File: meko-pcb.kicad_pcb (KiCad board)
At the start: 2 copper layers, 258.5 x 149 mm, 60 parts, among them IC1 ES9218PQ, IC2 AS5600-ASOM, IC3 LP5912-3.3DRVR, J1 GDEY0154D67, J2 MEM2090-00-145-00-A, J3 USB_C_Receptacle_USB2.0_16P, J4 Conn_ARM_SWD_TagConnect_TC2030, J5 SJ2-35954B-SMT-TR, Q1 SS8050, Q2 SS8050, Q3 Si1308EDL, U1 ESP32-PICO-MINI-02, U12 BQ24075RGT, U2 LP5907SNX-1.8/NOPB, U3 LP5907SNX-3.3/NOPB, U5 USBLC6-2SC6, U6 LP5907SNX-3.3/NOPB, U7 LP5907SNX-3.3/NOPB, U8 CP2102N-Axx-xQFN24, Y2 ECS-2520SMV-500-GP-TR

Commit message: esd, jack, io expander, led, power swquence
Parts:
- removed J4: Conn_ARM_SWD_TagConnect_TC2030, Connector:Tag-Connect_TC2030-IDC-FP_2x03_P1.27mm_Vertical
- removed JP9: SolderJumper_2_Bridged, Jumper:SolderJumper-2_P1.3mm_Bridged_RoundedPad1.0x1.5mm
- removed TP12, TP13, TP14: TestPoint, TestPoint:TestPoint_Pad_D1.5mm
- added D10: D_TVS, Diode_SMD:D_0201_0603Metric, F.Cu at (228.7, 158.2)
- added D11: D_TVS, Diode_SMD:D_0201_0603Metric, F.Cu at (228.7, 160.0)
- added D5: D3V3X8U9LP3810, Package_DFN_QFN:Diodes_UDFN3810-9_TYPE_B, F.Cu at (174.0, 52.0)
- added D6: D3V3X8U9LP3810, Package_DFN_QFN:Diodes_UDFN3810-9_TYPE_B, F.Cu at (177.1, 52.0)
- added D7: SK6805, LED_SMD:LED_SK6805_PLCC4_2.4x2.7mm_P1.3mm, F.Cu at (148.5, 151.3)
- added D8: D_TVS, Diode_SMD:D_0201_0603Metric, F.Cu at (203.2, 135.0)
- added D9: D_TVS, Diode_SMD:D_0201_0603Metric, F.Cu at (228.7, 156.5)
- added IC4: TCAL9538RSVR, TCAL9538RSVR:QFN40P180X260X55-16N, F.Cu at (180.5, 51.6)
- added JP10: SolderJumper_2_Open, Jumper:SolderJumper-2_P1.3mm_Open_RoundedPad1.0x1.5mm, F.Cu at (174.5, 69.5)
- added U4: LP5907SNX-1.8/NOPB, Package_SON:Texas_X2SON-4_1x1mm_P0.65mm, F.Cu at (178.3, 61.9)
- JP2, JP3, JP4: value SolderJumper_2_Bridged -> SolderJumper_2_Open; footprint Jumper:SolderJumper-2_P1.3mm_Bridged_RoundedPad1.0x1.5mm -> Jumper:SolderJumper-2_P1.3mm_Open_RoundedPad1.0x1.5mm
- moved TP11 110.5 mm to (180.3, 55.8)
- moved JP4 97.9 mm to (183.9, 62.4)
- moved JP2 87.4 mm to (174.5, 62.4)
- moved JP3 87.4 mm to (174.5, 65.9)
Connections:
- net /HAL_SCL renamed /I2C_1_SCL
- net /HAL_SDA renamed /I2C_1_SDA
- net /USB/SUSP renamed /PWR_EN_USB
- IC1 pad 22: Net-(IC1-OUT_L) -> /audio/OUT_L
- IC1 pad 9: Net-(IC1-OUT_R) -> /audio/OUT_R
- J1 pad 18: Net-(J1-VDD) -> /DISPL_VDD
- J1 pad 19: unconnected-(J1-VPP-Pad19) -> /DISPL_VPP
- J1 pad 6: unconnected-(J1-TSCL-Pad6) -> /DISPL_TSCL
- J1 pad 7: unconnected-(J1-TSDA-Pad7) -> /DISPL_TSDA
- J3 pad S1: GND -> unconnected-(J3-SHIELD-PadS1)_3
- J5 pad R1: Net-(J5-PadR1) -> /audio/OUT_R
- J5 pad R2: Net-(J5-PadR1) -> GND
- J5 pad S: Net-(J5-PadR1) -> /AUDIO_MIC
- J5 pad T: Net-(J5-PadR1) -> /audio/OUT_L
- J5 pad TN: Net-(J5-PadR1) -> /AUDIO_TN
- JP1 pad 1: /power/EN3V3VCAA -> /power/EN3V3MCLK
- JP2 pad 1: /power/EN3V3MCLK -> /power/REG-OUT
- JP2 pad 2: /power/REG-OUT -> /PWR_EN3V3AVCC
- JP3 pad 1: /power/EN3V3AVCC -> +3V3AVCC
- JP3 pad 2: /power/REG-OUT -> /PWR_EN1V8AVCC
- JP4 pad 1: /power/EN1V8AVCC -> +3V3MCLK
- JP4 pad 2: +3V3AVCC -> /AUDIO_MLCK_EN
- L1 pad 1: +3V3AVCC -> +3V3
- TP11 pad 1: /power/EN1V8AVCC -> /power/EN3V3MCLK
- U1 pad 12: unconnected-(U1-32K_XP/GPIO32/ADC1_CH4-Pad12) -> /EXP_~{INT}
- U1 pad 13: /AUDIO_MLCK_EN -> /HAPTIC_MOTOR
- U1 pad 29: /BTN_SIDE_R -> /EXP_~{RES}
- U1 pad 6: /BTN_SIDE_L -> /AUDIO_MIC
- U1 pad 7: /AUDIO_RESETB -> /LED
- U2 pad 3: /power/EN1V8AVCC -> /PWR_EN1V8AVCC
- U3 pad 3: /power/EN3V3VCAA -> /PWR_EN3V3VCCA
- U7 pad 3: /power/EN3V3AVCC -> /PWR_EN3V3AVCC

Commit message: small fixes
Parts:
- added D1: US1B, Diode_SMD:D_SMA, F.Cu at (204.0, 138.5)
- added Q3: SS8050, Package_TO_SOT_SMD:SOT-23, F.Cu at (114.6, 86.0)
- renumbered C94 to C23, C93 to C24, C92 to C25, C1 to C26, D9 to D11, D8 to D12, D7 to D2, D4 to D3, D3 to D4, D2 to D5, D5 to D6, D6 to D7, D1 to D8, D11 to D9, F2 to F1, IC2 to IC1, IC4 to IC2, IC1 to IC4, J5 to J4, JP7 to JP1, JP8 to JP2, JP6 to JP3, JP5 to JP4, JP1 to JP5, JP10 to JP6, JP2 to JP7, JP3 to JP8, JP4 to JP9, L2 to L1, L1 to L2, Q3 to Q4, R34 to R16, R32 to R17, R30 to R19, R28 to R20, R11 to R25, R12 to R26, TP3 to TP1, TP1 to TP10, TP2 to TP11, TP7 to TP2, TP4 to TP3, TP5 to TP4, TP8 to TP5, TP11 to TP7, TP9 to TP8, TP10 to TP9, U12 to U2, U6 to U3, U3 to U4, U4 to U5, U7 to U6, U2 to U7, U5 to U8, U8 to U9, Y2 to Y1

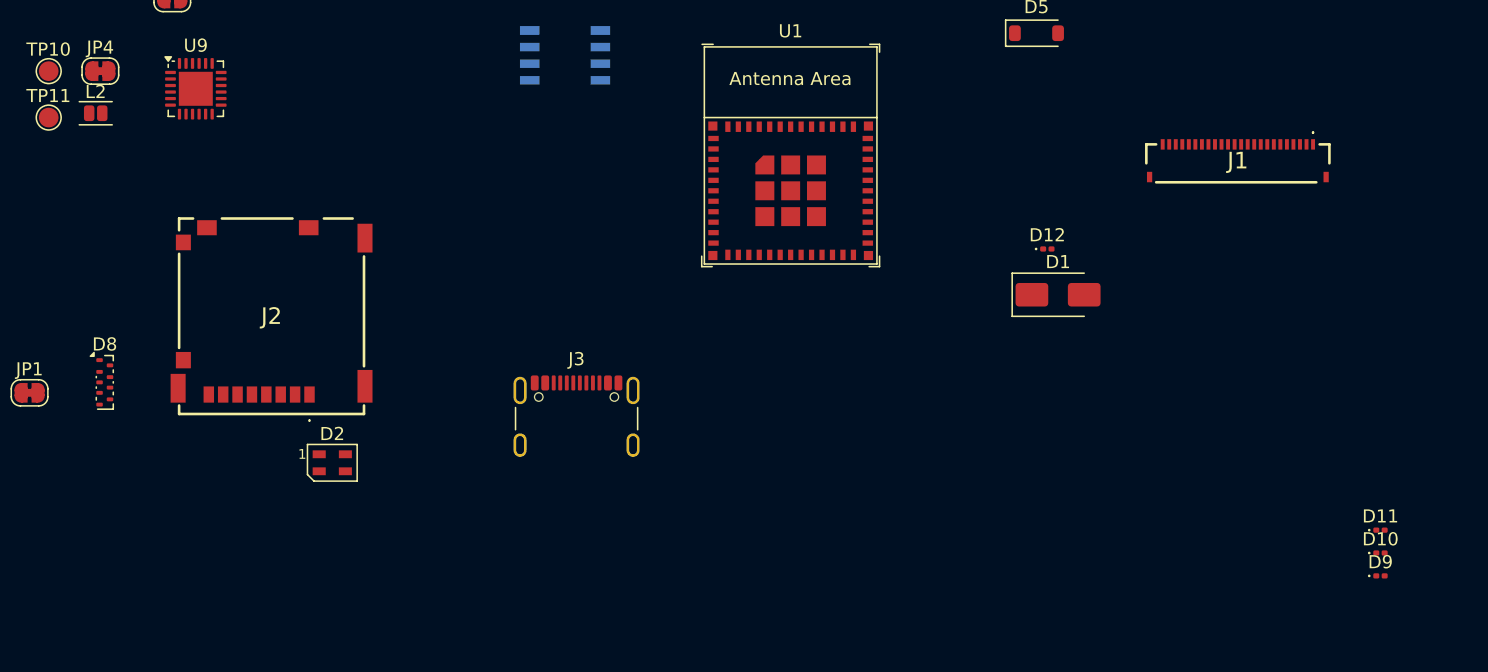
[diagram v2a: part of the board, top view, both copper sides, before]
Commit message: added 3d models
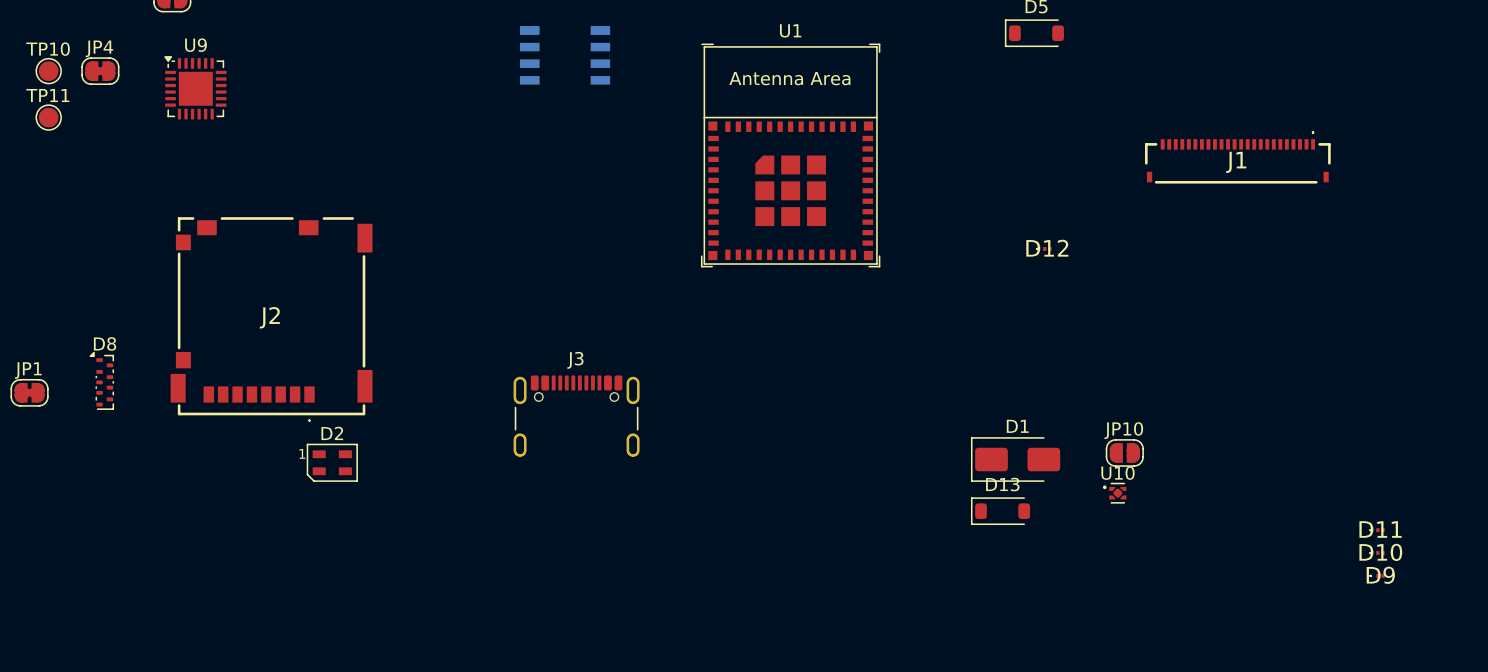
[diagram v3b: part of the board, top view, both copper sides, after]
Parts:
- removed L2: 100uH, Inductor_SMD:L_TDK_MLZ2012_h1.25mm
- added D13: MBR0530, Diode_SMD:D_SOD-123, F.Cu at (199.8, 155.1)
- added JP10: SolderJumper_2_Open, Jumper:SolderJumper-2_P1.3mm_Open_RoundedPad1.0x1.5mm, F.Cu at (209.1, 150.6)
- added U10: LP5907SNX-1.8/NOPB, Package_SON:Texas_X2SON-4_1x1mm_P0.65mm, F.Cu at (208.6, 153.7)
- D10, D11, D12, D9: footprint Diode_SMD:D_0201_0603Metric -> CD0201-T2.0LC:CD0201T20LC
- moved D1 13.0 mm to (200.9, 151.1)
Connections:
- IC1 pad 6: /I2C_1_SDA -> /I2C_SDA
- IC1 pad 7: /I2C_1_SCL -> /I2C_SCL
- IC2 pad 10: /BTN_SIDE_R -> /PWR_EN3V3AVDD
- IC2 pad 12: /I2C_1_SCL -> /I2C_SCL
- IC2 pad 13: /I2C_1_SDA -> /I2C_SDA
- IC2 pad 5: /BTN_SIDE_L -> unconnected-(IC2-P3-Pad5)
- IC4 pad 38: /AUDIO_SCL -> /I2C_SCL
- IC4 pad 39: /AUDIO_SDA -> /I2C_SDA
- Q2 pad 3: /AUDIO_DATA_CLK -> Net-(D13-A)
- U1 pad 26: /I2C_1_SDA -> /I2C_SDA
- U1 pad 33: /I2C_1_SCL -> /I2C_SCL
- U1 pad 34: /AUDIO_DATA_2 -> /BTN_SIDE_L
- U1 pad 35: /AUDIO_DATA1 -> /BTN_SIDE_R

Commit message: fuel gauge ic
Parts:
- added IC5: BQ27427YZFR, BQ27427YZFR:BGA9C50P3X3_158X162X62, F.Cu at (145.5, 67.0)
- added R31: 10k, Resistor_SMD:R_0402_1005Metric, F.Cu at (144.6, 70.3)
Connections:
- net /power/VBAT renamed +BATT
- D13 pad 1: /AUDIO_DATA_CLK -> /AUDIO_DATA_CLK/BOOT
- IC2 pad 5: unconnected-(IC2-P3-Pad5) -> /PWR_FUEL_GPOUT
- U1 pad 15: /AUDIO_SCL -> /AUDIO_DATA1
- U1 pad 16: /AUDIO_SDA -> /AUDIO_DATA1
- U1 pad 23: /AUDIO_DATA_CLK -> /AUDIO_DATA_CLK/BOOT
- U1 pad 27: /MEM_COM -> /LED
- U1 pad 7: /LED -> /MEM_COM

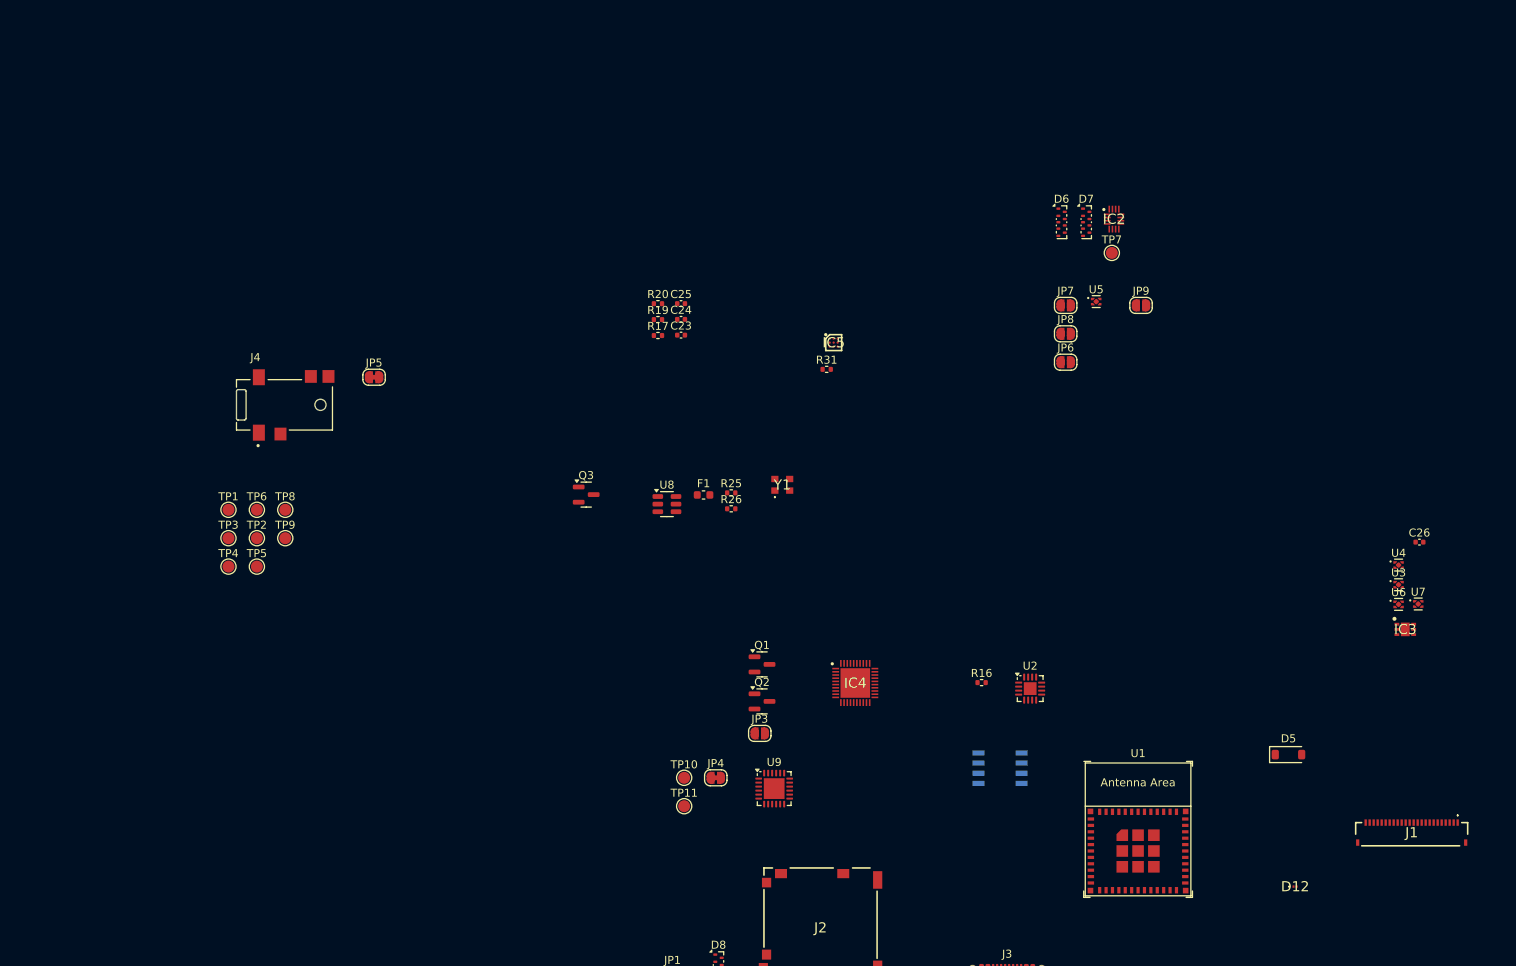
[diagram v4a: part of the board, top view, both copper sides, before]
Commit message: added missing 3d models
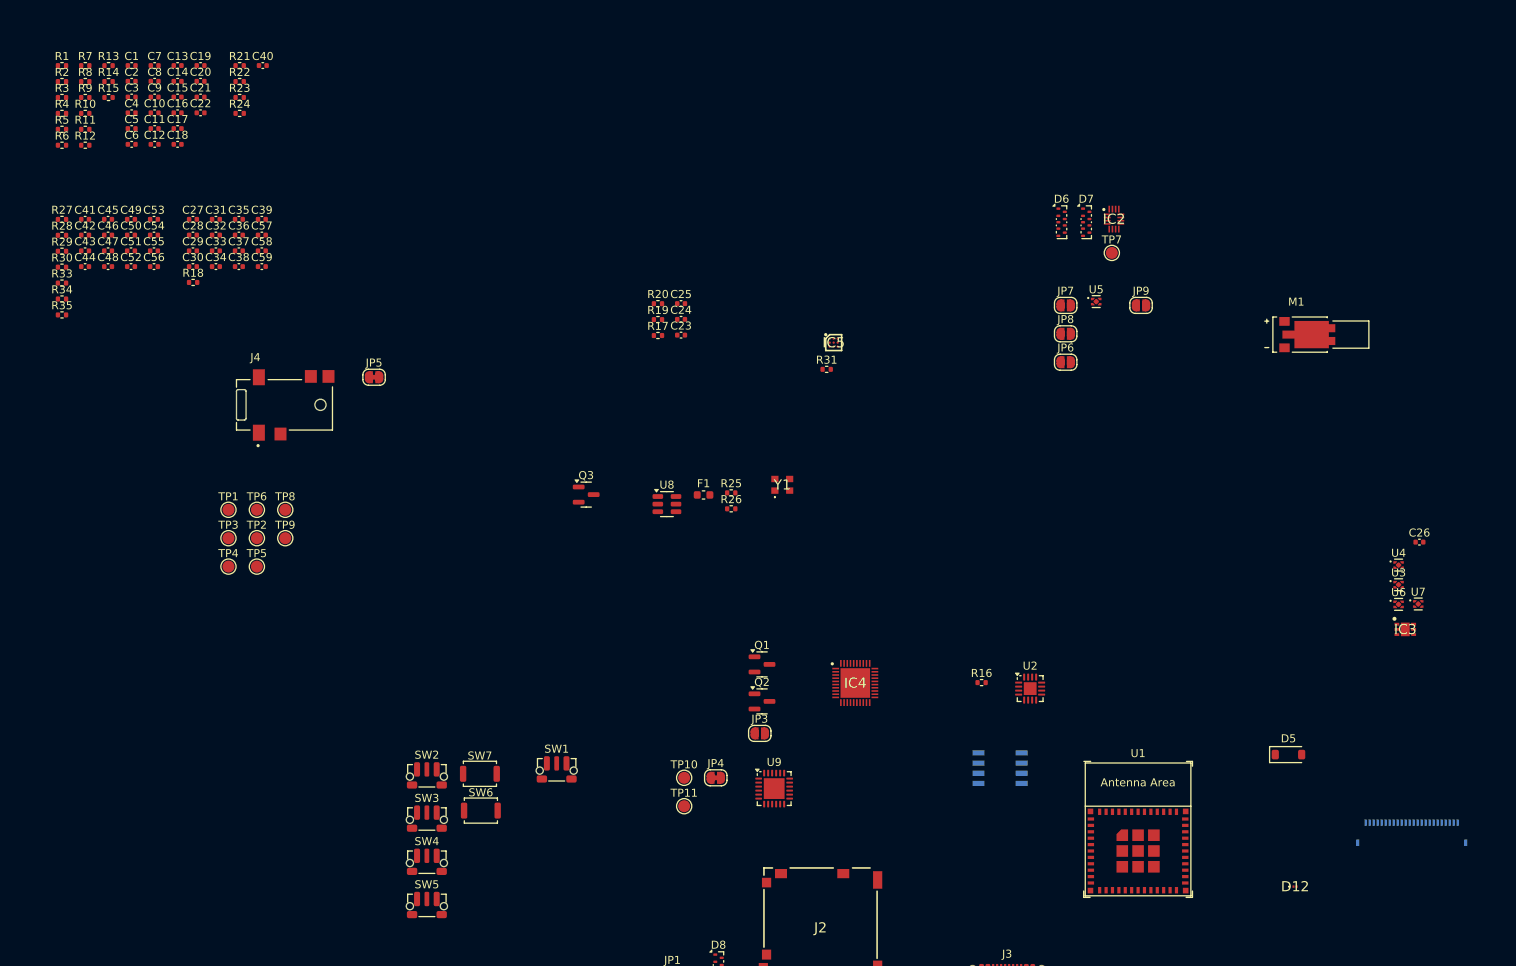
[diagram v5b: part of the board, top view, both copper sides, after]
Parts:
- added C1: 100nF, Capacitor_SMD:C_0402_1005Metric, F.Cu at (57.8, 32.4)
- added C10: 1uF, Capacitor_SMD:C_0402_1005Metric, F.Cu at (60.6, 38.3)
- added C11: 1uF, Capacitor_SMD:C_0402_1005Metric, F.Cu at (60.6, 40.2)
- added C12: 1uF, Capacitor_SMD:C_0402_1005Metric, F.Cu at (60.6, 42.2)
- added C13: 1uF, Capacitor_SMD:C_0402_1005Metric, F.Cu at (63.5, 32.4)
- added C14: 1uF, Capacitor_SMD:C_0402_1005Metric, F.Cu at (63.5, 34.3)
- added C15: 1uF, Capacitor_SMD:C_0402_1005Metric, F.Cu at (63.5, 36.3)
- added C16: 1uF, Capacitor_SMD:C_0402_1005Metric, F.Cu at (63.5, 38.3)
- added C17: 1uF, Capacitor_SMD:C_0402_1005Metric, F.Cu at (63.5, 40.2)
- added C18: 1uF, Capacitor_SMD:C_0402_1005Metric, F.Cu at (63.5, 42.2)
- added C19: 1uF, Capacitor_SMD:C_0402_1005Metric, F.Cu at (66.4, 32.4)
- added C2: 100nF, Capacitor_SMD:C_0402_1005Metric, F.Cu at (57.8, 34.3)
- added C20: 1uF, Capacitor_SMD:C_0402_1005Metric, F.Cu at (66.4, 34.3)
- added C21: 1uF, Capacitor_SMD:C_0402_1005Metric, F.Cu at (66.4, 36.3)
- added C22: 1uF, Capacitor_SMD:C_0402_1005Metric, F.Cu at (66.4, 38.3)
- added C27: 1uF, Capacitor_SMD:C_0402_1005Metric, F.Cu at (65.4, 51.6)
- added C28: 1uF, Capacitor_SMD:C_0402_1005Metric, F.Cu at (65.4, 53.6)
- added C29: 1uF, Capacitor_SMD:C_0402_1005Metric, F.Cu at (65.4, 55.5)
- added C3: 100nF, Capacitor_SMD:C_0402_1005Metric, F.Cu at (57.8, 36.3)
- added C30: 1uF, Capacitor_SMD:C_0402_1005Metric, F.Cu at (65.4, 57.5)
- added C31: 1uF, Capacitor_SMD:C_0402_1005Metric, F.Cu at (68.3, 51.6)
- added C32: 1uF, Capacitor_SMD:C_0402_1005Metric, F.Cu at (68.3, 53.6)
- added C33: 1uF, Capacitor_SMD:C_0402_1005Metric, F.Cu at (68.3, 55.5)
- added C34: 1uF, Capacitor_SMD:C_0402_1005Metric, F.Cu at (68.3, 57.5)
- added C35: 1uF, Capacitor_SMD:C_0402_1005Metric, F.Cu at (71.2, 51.6)
- added C36: 1uF, Capacitor_SMD:C_0402_1005Metric, F.Cu at (71.2, 53.6)
- added C37: 1uF, Capacitor_SMD:C_0402_1005Metric, F.Cu at (71.2, 55.5)
- added C38: 1uF, Capacitor_SMD:C_0402_1005Metric, F.Cu at (71.2, 57.5)
- added C39: 1uF, Capacitor_SMD:C_0402_1005Metric, F.Cu at (74.0, 51.6)
- added C4: 100nF, Capacitor_SMD:C_0402_1005Metric, F.Cu at (57.8, 38.3)
- added C40: 10uF, Capacitor_SMD:C_0402_1005Metric, F.Cu at (74.1, 32.4)
- added C41: 1uF, Capacitor_SMD:C_0402_1005Metric, F.Cu at (51.9, 51.6)
- added C42: 22uF, Capacitor_SMD:C_0402_1005Metric, F.Cu at (51.9, 53.6)
- added C43: 1uF, Capacitor_SMD:C_0402_1005Metric, F.Cu at (51.9, 55.5)
- added C44: 1uF, Capacitor_SMD:C_0402_1005Metric, F.Cu at (51.9, 57.5)
- added C45: 1uF, Capacitor_SMD:C_0402_1005Metric, F.Cu at (54.8, 51.6)
- added C46: 4.7uF, Capacitor_SMD:C_0402_1005Metric, F.Cu at (54.8, 53.6)
- added C47: 4.7uF, Capacitor_SMD:C_0402_1005Metric, F.Cu at (54.8, 55.5)
- added C48: 4.7uF, Capacitor_SMD:C_0402_1005Metric, F.Cu at (54.8, 57.5)
- added C49: 4.7uF, Capacitor_SMD:C_0402_1005Metric, F.Cu at (57.7, 51.6)
- added C5: 100nF, Capacitor_SMD:C_0402_1005Metric, F.Cu at (57.8, 40.2)
- added C50: 4.7uF, Capacitor_SMD:C_0402_1005Metric, F.Cu at (57.7, 53.6)
- added C51: 2.2uF, Capacitor_SMD:C_0402_1005Metric, F.Cu at (57.7, 55.5)
- added C52: 1uF, Capacitor_SMD:C_0402_1005Metric, F.Cu at (57.7, 57.5)
- added C53: 2.2nF, Capacitor_SMD:C_0402_1005Metric, F.Cu at (60.5, 51.6)
- added C54: 2.2nF, Capacitor_SMD:C_0402_1005Metric, F.Cu at (60.5, 53.6)
- added C55: 2.2nF, Capacitor_SMD:C_0402_1005Metric, F.Cu at (60.5, 55.5)
- added C56: 2.2nF, Capacitor_SMD:C_0402_1005Metric, F.Cu at (60.5, 57.5)
- added C57: 1uF, Capacitor_SMD:C_0402_1005Metric, F.Cu at (74.0, 53.6)
- added C58: 1uF, Capacitor_SMD:C_0402_1005Metric, F.Cu at (74.0, 55.5)
- added C59: 1uF, Capacitor_SMD:C_0402_1005Metric, F.Cu at (74.0, 57.5)
- added C6: 100nF, Capacitor_SMD:C_0402_1005Metric, F.Cu at (57.8, 42.2)
- added C7: 100nF, Capacitor_SMD:C_0402_1005Metric, F.Cu at (60.6, 32.4)
- added C8: 100nF, Capacitor_SMD:C_0402_1005Metric, F.Cu at (60.6, 34.3)
- added C9: 1uF, Capacitor_SMD:C_0402_1005Metric, F.Cu at (60.6, 36.3)
- added M1: HD-EMB1204-SM, HD-EMB1204-SM:PUI_HD-EMB1204-SM, F.Cu at (203.8, 66.0)
- added R1: 10k, Resistor_SMD:R_0402_1005Metric, F.Cu at (49.0, 32.4)
- added R10: 10k, Resistor_SMD:R_0402_1005Metric, F.Cu at (52.0, 38.4)
- added R11: 10k, Resistor_SMD:R_0402_1005Metric, F.Cu at (52.0, 40.3)
- added R12: 1M, Resistor_SMD:R_0402_1005Metric, F.Cu at (52.0, 42.3)
- added R13: 2.2R, Resistor_SMD:R_0402_1005Metric, F.Cu at (54.9, 32.4)
- added R14: 10k, Resistor_SMD:R_0402_1005Metric, F.Cu at (54.9, 34.4)
- added R15: 10k, Resistor_SMD:R_0402_1005Metric, F.Cu at (54.9, 36.4)
- added R18: 10k, Resistor_SMD:R_0402_1005Metric, F.Cu at (65.4, 59.5)
- added R2: 10k, Resistor_SMD:R_0402_1005Metric, F.Cu at (49.0, 34.4)
- added R21: 10k, Resistor_SMD:R_0402_1005Metric, F.Cu at (71.2, 32.4)
- added R22: 10k, Resistor_SMD:R_0402_1005Metric, F.Cu at (71.2, 34.4)
- added R23: 10k, Resistor_SMD:R_0402_1005Metric, F.Cu at (71.2, 36.4)
- added R24: 10k, Resistor_SMD:R_0402_1005Metric, F.Cu at (71.2, 38.4)
- added R27: 10k, Resistor_SMD:R_0402_1005Metric, F.Cu at (49.0, 51.6)
- added R28: 47k, Resistor_SMD:R_0402_1005Metric, F.Cu at (49.0, 53.6)
- added R29: 47k, Resistor_SMD:R_0402_1005Metric, F.Cu at (49.0, 55.6)
- added R3: 10k, Resistor_SMD:R_0402_1005Metric, F.Cu at (49.0, 36.4)
- added R30: 47k, Resistor_SMD:R_0402_1005Metric, F.Cu at (49.0, 57.6)
- added R33: 10k, Resistor_SMD:R_0402_1005Metric, F.Cu at (49.0, 59.6)
- added R34: 1.8k, Resistor_SMD:R_0402_1005Metric, F.Cu at (49.0, 61.5)
- added R35: 10k, Resistor_SMD:R_0402_1005Metric, F.Cu at (49.0, 63.5)
- added R4: 10k, Resistor_SMD:R_0402_1005Metric, F.Cu at (49.0, 38.4)
- added R5: 10k, Resistor_SMD:R_0402_1005Metric, F.Cu at (49.0, 40.3)
- added R6: 10k, Resistor_SMD:R_0402_1005Metric, F.Cu at (49.0, 42.3)
- added R7: 10k, Resistor_SMD:R_0402_1005Metric, F.Cu at (52.0, 32.4)
- added R8: 10k, Resistor_SMD:R_0402_1005Metric, F.Cu at (52.0, 34.4)
- added R9: 1k, Resistor_SMD:R_0402_1005Metric, F.Cu at (52.0, 36.4)
- added SW1: SW_Push, Button_Switch_SMD:SW_Push_1P1T-MP_NO_Horizontal_Alps_SKRTLAE010, F.Cu at (110.9, 120.5)
- added SW2: SW_Push, Button_Switch_SMD:SW_Push_1P1T-MP_NO_Horizontal_Alps_SKRTLAE010, F.Cu at (94.7, 121.2)
- added SW3: SW_Push, Button_Switch_SMD:SW_Push_1P1T-MP_NO_Horizontal_Alps_SKRTLAE010, F.Cu at (94.7, 126.7)
- added SW4: SW_Push, Button_Switch_SMD:SW_Push_1P1T-MP_NO_Horizontal_Alps_SKRTLAE010, F.Cu at (94.7, 132.1)
- added SW5: SW_Push, Button_Switch_SMD:SW_Push_1P1T-MP_NO_Horizontal_Alps_SKRTLAE010, F.Cu at (94.7, 137.4)
- added SW6: SW_Push, Button_Switch_SMD:SW_Push_SPST_NO_Alps_SKRK, F.Cu at (101.4, 125.5)
- added SW7: SW_Push, Button_Switch_SMD:SW_Push_SPST_NO_Alps_SKRK, F.Cu at (101.3, 120.9)
- J1: moved to B.Cu
- turned J1 to 180 degrees

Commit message: small stuff
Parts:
- added TP12: TestPoint, TestPoint:TestPoint_Pad_D1.5mm, F.Cu at (22.9, 117.5)
- added TP13: TestPoint, TestPoint:TestPoint_Pad_D1.5mm, F.Cu at (22.9, 121.0)
- added TP14: TestPoint, TestPoint:TestPoint_Pad_D1.5mm, F.Cu at (22.9, 124.6)
- added TP15: TestPoint, TestPoint:TestPoint_Pad_D1.5mm, F.Cu at (22.9, 128.2)
- added TP16: TestPoint, TestPoint:TestPoint_Pad_D1.5mm, F.Cu at (26.5, 117.5)
- added TP17: TestPoint, TestPoint:TestPoint_Pad_D1.5mm, F.Cu at (26.5, 121.0)
- added TP18: TestPoint, TestPoint:TestPoint_Pad_D1.5mm, F.Cu at (26.5, 124.6)
- added TP19: TestPoint, TestPoint:TestPoint_Pad_D1.5mm, F.Cu at (32.0, 117.5)
- added TP20: TestPoint, TestPoint:TestPoint_Pad_D1.5mm, F.Cu at (32.0, 121.0)
- moved D4 79.8 mm to (179.7, 81.4)
- moved JP2 79.8 mm to (174.6, 85.1)
- moved L1 79.8 mm to (174.2, 88.3)
- moved Q4 79.8 mm to (179.0, 88.5)
- moved D3 79.8 mm to (179.7, 84.8)
- moved U1 76.8 mm to (137.7, 68.9), turned to 90 degrees
- moved D13 73.7 mm to (154.1, 97.2)
- moved SW7 73.7 mm to (55.6, 63.1)
- moved TP10 73.7 mm to (81.1, 63.6)
- moved D12 73.7 mm to (157.5, 77.2)
- moved D2 73.7 mm to (102.8, 93.5)
- moved F1 73.7 mm to (83.5, 28.2)
- moved IC1 73.7 mm to (120.6, 62.4)
- moved J2 73.7 mm to (98.2, 82.3)
- moved J3 73.7 mm to (121.5, 91.1)
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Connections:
- IC4 pad 36: /AUDIO_DATA_CLK -> /AUDIO_DATA_CLK/BOOT
- R30 pad 1: /AUDIO_DATA_CLK -> /AUDIO_DATA_CLK/BOOT
- U1 pad 15: /AUDIO_DATA1 -> /I2C_SCL
- U1 pad 16: /AUDIO_DATA1 -> /I2C_SDA
- U1 pad 26: /I2C_SDA -> /AUDIO_DATA_2
- U1 pad 33: /I2C_SCL -> /AUDIO_DATA1
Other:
- board size 258.5 x 149 mm -> 225.5 x 158 mm
